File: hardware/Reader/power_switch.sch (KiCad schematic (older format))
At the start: 8 parts, among them Q13 IRLML5103TRPBF, Q14 IRLML5103TRPBF, Q15 IRLML5103TRPBF, Q16 NX7002AK,215

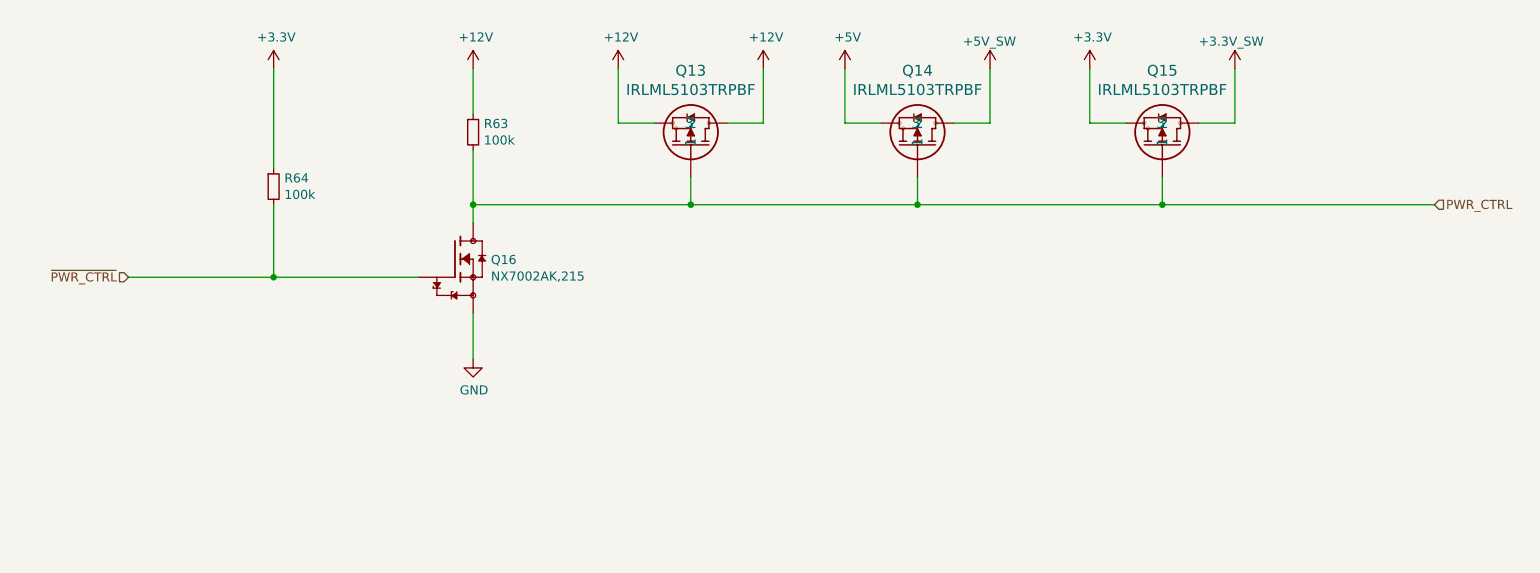
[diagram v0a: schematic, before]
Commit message: Completed schematics for reader
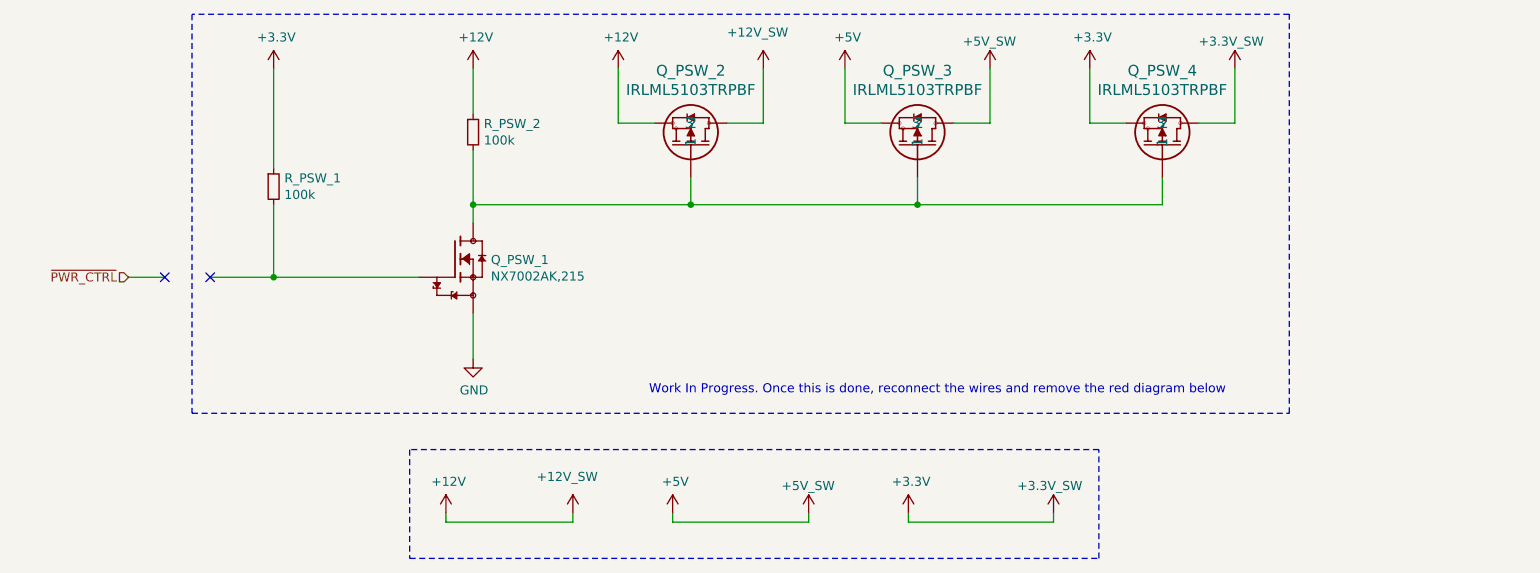
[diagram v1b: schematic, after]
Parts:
- removed PWR?: +3.3V_SW, symbol CANtech:+3.3V_SW
- removed PWR?: +5V_SW, symbol CANtech:+5V_SW
- Q_PSW_1: renamed from Q16; footprint SOT95P230X110-3N -> footprints:SOT95P230X110-3N
- Q_PSW_2: renamed from Q13; footprint MICRO3_SOT23_INF -> footprints:IRLML5103TRPBF
- Q_PSW_3: renamed from Q14; footprint MICRO3_SOT23_INF -> footprints:IRLML5103TRPBF
- Q_PSW_4: renamed from Q15; footprint MICRO3_SOT23_INF -> footprints:IRLML5103TRPBF
- R_PSW_1: renamed from R64; footprint (none) -> footprints:RESC1608X55N; Part Name (none) -> RT0603DRE07100KL
- R_PSW_2: renamed from R63; footprint (none) -> footprints:RESC1608X55N; Part Name (none) -> RT0603DRE07100KL
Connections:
- net +3V3 is gone; now on net +3.3V_SW: Q_PSW_4.3, R_PSW_1.1
- net +5V_SW is gone; now on net +5V: Q_PSW_3.2
- net ~PWR_CTRL~: no longer Q_PSW_1.1, R_PSW_1.2
- net PWR_CTRL: no longer names the net of Q_PSW_1.3, Q_PSW_2.1, Q_PSW_3.1, Q_PSW_4.1, R_PSW_2.2
- new net: Q_PSW_1.1, R_PSW_1.2
- no-connect marks 0 -> 2
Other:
- note added: "Work In Progress. Once this is done, reconnect the wires and remove the red diagram below"
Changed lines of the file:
@@
 $Descr USLetter 11000 8500
 encoding utf-8
-Sheet 8 9
-Title ""
-Date ""
-Rev ""
-Comp ""
-Comment1 ""
-Comment2 ""
+Sheet 7 17
+Title "CANnect Reader | Power Switch"
+Date "2020-10-20"
+Rev "0.0.1"
+Comp "CANtech"
+Comment1 "Created by Choong Jin Ng | jin8383@gmail.com"
+Comment2 "Taken from STN21xx's datasheet for recommended configuration"
 Comment3 ""
-Comment4 ""
+Comment4 "Component Identifier: PSW"
 $EndDescr
 Text HLabel 1550 3000 0    50   Input ~ 0
@@
 P 5900 2450
 AR Path="/5F8ADA45/5FA57921" Ref="MOSFET?"  Part="1"
-AR Path="/5FA56A4E/5FA57921" Ref="Q14"  Part="1"
-F 0 "Q14" V 6489 2450 60  0000 C CNN
+AR Path="/5FA56A4E/5FA57921" Ref="Q_PSW_3"  Part="1"
+F 0 "Q_PSW_3" V 6489 2450 60  0000 C CNN
 F 1 "IRLML5103TRPBF" V 6383 2450 60  0000 C CNN
-F 2 "MICRO3_SOT23_INF" H 6350 2190 60  0001 C CNN
+F 2 "footprints:IRLML5103TRPBF" H 6350 2190 60  0001 C CNN
 F 3 "" H 5900 2450 60  0000 C CNN
 	1    5900 2450
@@
 P 7250 2450
 AR Path="/5F8ADA45/5FA57927" Ref="MOSFET?"  Part="1"
-AR Path="/5FA56A4E/5FA57927" Ref="Q15"  Part="1"
-F 0 "Q15" V 7839 2450 60  0000 C CNN
+AR Path="/5FA56A4E/5FA57927" Ref="Q_PSW_4"  Part="1"
+F 0 "Q_PSW_4" V 7839 2450 60  0000 C CNN
 F 1 "IRLML5103TRPBF" V 7733 2450 60  0000 C CNN
-F 2 "MICRO3_SOT23_INF" H 7700 2190 60  0001 C CNN
+F 2 "footprints:IRLML5103TRPBF" H 7700 2190 60  0001 C CNN
 F 3 "" H 7250 2450 60  0000 C CNN
 	1    7250 2450
 	0    1    -1   0
 $EndComp
-Text HLabel 8750 2600 2    50   Input ~ 0
-PWR_CTRL
-$Comp
-L NX7002AK_215:NX7002AK,215 Q16
+$Comp
+L NX7002AK_215:NX7002AK,215 Q_PSW_1
 U 1 1 5FA59B13
 P 3350 2900
-F 0 "Q16" H 3548 2896 50  0000 L CNN
+F 0 "Q_PSW_1" H 3548 2896 50  0000 L CNN
 F 1 "NX7002AK,215" H 3548 2805 50  0000 L CNN
-F 2 "SOT95P230X110-3N" H 3350 2900 50  0001 L BNN
+F 2 "footprints:SOT95P230X110-3N" H 3350 2900 50  0001 L BNN
 F 3 "1.1mm" H 3350 2900 50  0001 L BNN
 F 4 "Nexperia" H 3350 2900 50  0001 L BNN "Field4"
@@
 $EndComp
 $Comp
-L Device:R_Small R63
+L Device:R_Small R_PSW_2
 U 1 1 5FA5B8B4
 P 3450 2200
-F 0 "R63" H 3509 2246 50  0000 L CNN
+F 0 "R_PSW_2" H 3509 2246 50  0000 L CNN
 F 1 "100k" H 3509 2155 50  0000 L CNN
-F 2 "" H 3450 2200 50  0001 C CNN
-F 3 "~" H 3450 2200 50  0001 C CNN
+F 2 "footprints:RESC1608X55N" H 3450 2200 50  0001 C CNN
+F 3 "https://www.yageo.com/upload/media/product/productsearch/datasheet/rchip/PYu-RT_1-to-0.01_RoHS_L_12.pdf" H 3450 2200 50  0001 C CNN
+F 4 "RT0603DRE07100KL" H 3450 2200 50  0001 C CNN "Part Name"
 	1    3450 2200
 	1    0    0    -1
 $EndComp
 $Comp
-L Device:R_Small R64
+L Device:R_Small R_PSW_1
 U 1 1 5FA5BF09
 P 2350 2500
-F 0 "R64" H 2409 2546 50  0000 L CNN
+F 0 "R_PSW_1" H 2409 2546 50  0000 L CNN
 F 1 "100k" H 2409 2455 50  0000 L CNN
-F 2 "" H 2350 2500 50  0001 C CNN
-F 3 "~" H 2350 2500 50  0001 C CNN
+F 2 "footprints:RESC1608X55N" H 2350 2500 50  0001 C CNN
+F 3 "https://www.yageo.com/upload/media/product/productsearch/datasheet/rchip/PYu-RT_1-to-0.01_RoHS_L_12.pdf" H 2350 2500 50  0001 C CNN
+F 4 "RT0603DRE07100KL" H 2350 2500 50  0001 C CNN "Part Name"
 	1    2350 2500
 	1    0    0    -1
 $EndComp
 $Comp
-L power:+3.3V #PWR?
+L power:+3.3V #PWR0134
 U 1 1 5FA5C2C6
 P 2350 1850
-F 0 "#PWR?" H 2350 1700 50  0001 C CNN
+F 0 "#PWR0134" H 2350 1700 50  0001 C CNN
 F 1 "+3.3V" H 2365 2023 50  0000 C CNN
 F 2 "" H 2350 1850 50  0001 C CNN
@@
 $EndComp
 $Comp
-L power:+3.3V #PWR?
+L power:+3.3V #PWR0135
 U 1 1 5FA5C48B
 P 6850 1850
-F 0 "#PWR?" H 6850 1700 50  0001 C CNN
+F 0 "#PWR0135" H 6850 1700 50  0001 C CNN
 F 1 "+3.3V" H 6865 2023 50  0000 C CNN
 F 2 "" H 6850 1850 50  0001 C CNN
@@
 $EndComp
 Wire Wire Line
-	1550 3000 2350 3000
-Wire Wire Line
 	2350 3000 2350 2600
 Wire Wire Line
 	2350 2400 2350 1850
 $Comp
-L power:+12V #PWR?
+L power:+12V #PWR0136
 U 1 1 5FA5EBBC
 P 3450 1850
-F 0 "#PWR?" H 3450 1700 50  0001 C CNN
+F 0 "#PWR0136" H 3450 1700 50  0001 C CNN
 F 1 "+12V" H 3465 2023 50  0000 C CNN
 F 2 "" H 3450 1850 50  0001 C CNN
@@
 Wire Wire Line
 	2350 3000 3150 3000
-Connection ~ 2350 3000
-$Comp
-L power:GND #PWR?
+$Comp
+L power:GND #PWR0137
 U 1 1 5FA5FCA0
 P 3450 3450
-F 0 "#PWR?" H 3450 3200 50  0001 C CNN
+F 0 "#PWR0137" H 3450 3200 50  0001 C CNN
 F 1 "GND" H 3455 3277 50  0000 C CNN
 F 2 "" H 3450 3450 50  0001 C CNN
@@
 P 4650 2450
 AR Path="/5F8ADA45/5FA5791B" Ref="MOSFET?"  Part="1"
-AR Path="/5FA56A4E/5FA5791B" Ref="Q13"  Part="1"
-F 0 "Q13" V 5239 2450 60  0000 C CNN
+AR Path="/5FA56A4E/5FA5791B" Ref="Q_PSW_2"  Part="1"
+F 0 "Q_PSW_2" V 5239 2450 60  0000 C CNN
 F 1 "IRLML5103TRPBF" V 5133 2450 60  0000 C CNN
-F 2 "MICRO3_SOT23_INF" H 5100 2190 60  0001 C CNN
+F 2 "footprints:IRLML5103TRPBF" H 5100 2190 60  0001 C CNN
 F 3 "" H 4650 2450 60  0000 C CNN
 	1    4650 2450
@@
 Wire Wire Line
 	7250 2600 7250 2450
-Connection ~ 7250 2600
-Wire Wire Line
-	7250 2600 8750 2600
-$Comp
-L power:+12V #PWR?
-U 1 1 5FA63E83
-P 5050 1850
-F 0 "#PWR?" H 5050 1700 50  0001 C CNN
-F 1 "+12V" H 5065 2023 50  0000 C CNN
-F 2 "" H 5050 1850 50  0001 C CNN
-F 3 "" H 5050 1850 50  0001 C CNN
-	1    5050 1850
-	1    0    0    -1
-$EndComp
-$Comp
-L CANtech:+3.3V_SW PWR?
+$Comp
+L CANtech:+3.3V_SW #PWR0139
 U 1 1 5FA68E31
 P 7650 1850
-F 0 "PWR?" H 7650 2100 50  0001 C CNN
+F 0 "#PWR0139" H 7650 2100 50  0001 C CNN
 F 1 "+3.3V_SW" H 7450 2000 50  0000 L CNN
 F 2 "" H 6900 2650 50  0001 C CNN
@@
 $EndComp
 $Comp
-L CANtech:+5V_SW PWR?
+L CANtech:+5V_SW #PWR0140
 U 1 1 5FA69F1C
 P 6300 1850
-F 0 "PWR?" H 6300 2100 50  0001 C CNN
+F 0 "#PWR0140" H 6300 2100 50  0001 C CNN
 F 1 "+5V_SW" H 6150 2000 50  0000 L CNN
 F 2 "" H 5550 2650 50  0001 C CNN
@@
 	6850 2150 6850 1850
 $Comp
-L power:+5V #PWR?
+L power:+5V #PWR0141
 U 1 1 5FA6E79E
 P 5500 1850
-F 0 "#PWR?" H 5500 1700 50  0001 C CNN
+F 0 "#PWR0141" H 5500 1700 50  0001 C CNN
 F 1 "+5V" H 5515 2023 50  0000 C CNN
 F 2 "" H 5500 1850 50  0001 C CNN
@@
 $EndComp
 $Comp
-L power:+12V #PWR?
+L power:+12V #PWR0142
 U 1 1 5FA6E93A
 P 4250 1850
-F 0 "#PWR?" H 4250 1700 50  0001 C CNN
+F 0 "#PWR0142" H 4250 1700 50  0001 C CNN
 F 1 "+12V" H 4265 2023 50  0000 C CNN
 F 2 "" H 4250 1850 50  0001 C CNN
@@
 Wire Wire Line
 	5500 2150 5500 1850
+$Comp
+L CANtech:+12V_SW #PWR0145
+U 1 1 5FB0601D
+P 5050 1850
+F 0 "#PWR0145" H 5050 2100 50  0001 C CNN
+F 1 "+12V_SW" H 4850 2050 50  0000 L CNN
+F 2 "" H 4300 2650 50  0001 C CNN
+F 3 "" H 4300 2650 50  0001 C CNN
+	1    5050 1850
+	1    0    0    -1
+$EndComp
+Wire Wire Line
+	1550 3000 1750 3000
+Wire Wire Line
+	2350 3000 2000 3000
+Connection ~ 2350 3000
+NoConn ~ 1750 3000
+NoConn ~ 2000 3000
+Wire Notes Line
+	1900 1550 1900 3750
+Wire Notes Line
+	1900 3750 7950 3750
+Wire Notes Line
+	7950 3750 7950 1550
+Wire Notes Line
+	7950 1550 1900 1550
+Text Notes 7600 3650 2    50   ~ 0
+Work In Progress. Once this is done, reconnect the wires and remove the red diagram below
+$Comp
+L power:+12V #PWR0146
+U 1 1 5FF636E9
+P 3300 4300
+F 0 "#PWR0146" H 3300 4150 50  0001 C CNN
+F 1 "+12V" H 3315 4473 50  0000 C CNN
+F 2 "" H 3300 4300 50  0001 C CNN
+F 3 "" H 3300 4300 50  0001 C CNN
+	1    3300 4300
+	1    0    0    -1
+$EndComp
+$Comp
+L CANtech:+12V_SW #PWR0147
+U 1 1 5FF63872
+P 4000 4300
+F 0 "#PWR0147" H 4000 4550 50  0001 C CNN
+F 1 "+12V_SW" H 3800 4500 50  0000 L CNN
+F 2 "" H 3250 5100 50  0001 C CNN
+F 3 "" H 3250 5100 50  0001 C CNN
+	1    4000 4300
+	1    0    0    -1
+$EndComp
+$Comp
+L power:+5V #PWR0148
+U 1 1 5FF63A17
+P 4550 4300
+F 0 "#PWR0148" H 4550 4150 50  0001 C CNN
+F 1 "+5V" H 4565 4473 50  0000 C CNN
+F 2 "" H 4550 4300 50  0001 C CNN
+F 3 "" H 4550 4300 50  0001 C CNN
+	1    4550 4300
+	1    0    0    -1
+$EndComp
+$Comp
+L CANtech:+5V_SW #PWR0149
+U 1 1 5FF63B0E
+P 5300 4300
+F 0 "#PWR0149" H 5300 4550 50  0001 C CNN
+F 1 "+5V_SW" H 5150 4450 50  0000 L CNN
+F 2 "" H 4550 5100 50  0001 C CNN
+F 3 "" H 4550 5100 50  0001 C CNN
+	1    5300 4300
+	1    0    0    -1
+$EndComp
+$Comp
+L power:+3.3V #PWR0150
+U 1 1 5FF63C8E
+P 5850 4300
+F 0 "#PWR0150" H 5850 4150 50  0001 C CNN
+F 1 "+3.3V" H 5865 4473 50  0000 C CNN
+F 2 "" H 5850 4300 50  0001 C CNN
+F 3 "" H 5850 4300 50  0001 C CNN
+	1    5850 4300
+	1    0    0    -1
+$EndComp
+$Comp
+L CANtech:+3.3V_SW #PWR0151
+U 1 1 5FF63E6A
+P 6650 4300
+F 0 "#PWR0151" H 6650 4550 50  0001 C CNN
+F 1 "+3.3V_SW" H 6450 4450 50  0000 L CNN
+F 2 "" H 5900 5100 50  0001 C CNN
+F 3 "" H 5900 5100 50  0001 C CNN
+	1    6650 4300
+	1    0    0    -1
+$EndComp
+Wire Wire Line
+	5850 4300 5850 4350
+Wire Wire Line
+	5850 4350 6650 4350
+Wire Wire Line
+	6650 4350 6650 4300
+Wire Wire Line
+	4550 4300 4550 4350
+Wire Wire Line
+	4550 4350 5300 4350
+Wire Wire Line
+	5300 4350 5300 4300
+Wire Wire Line
+	3300 4300 3300 4350
+Wire Wire Line
+	3300 4350 4000 4350
+Wire Wire Line
+	4000 4350 4000 4300
+Wire Notes Line rgb(194, 0, 0)
+	3100 4550 6900 4550
+Wire Notes Line rgb(194, 0, 0)
+	6900 4550 6900 3950
+Wire Notes Line rgb(194, 0, 0)
+	6900 3950 3100 3950
+Wire Notes Line rgb(194, 0, 0)
+	3100 3950 3100 4550
 $EndSCHEMATC
